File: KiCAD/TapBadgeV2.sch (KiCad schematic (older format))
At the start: 15 parts, among them M101 G0832013D, U101 DRV2605

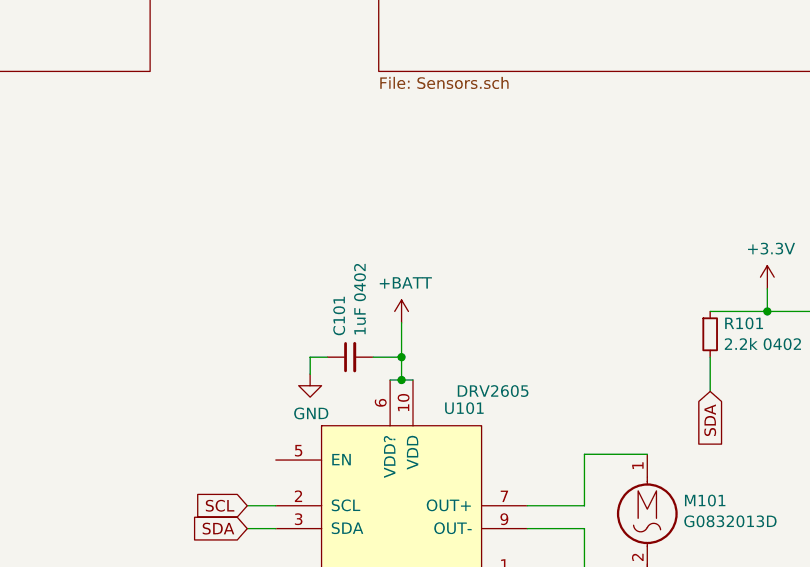
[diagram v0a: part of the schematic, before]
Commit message: Continue work on Schematics
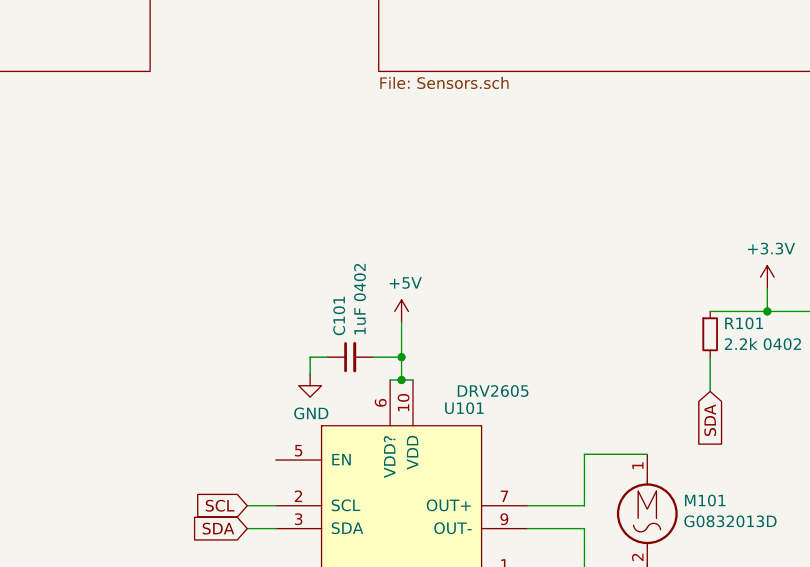
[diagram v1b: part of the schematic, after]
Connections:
- net +BATT renamed +5V
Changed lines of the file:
@@
 $Descr A4 11693 8268
 encoding utf-8
-Sheet 1 6
+Sheet 1 7
 Title ""
 Date ""
@@
 Wire Wire Line
 	7550 4800 7825 4800
-$Comp
-L power:+BATT #PWR0136
-U 1 1 60F9587F
-P 6750 4225
-F 0 "#PWR0136" H 6750 4075 50  0001 C CNN
-F 1 "+BATT" H 6765 4398 50  0000 C CNN
-F 2 "" H 6750 4225 50  0001 C CNN
-F 3 "" H 6750 4225 50  0001 C CNN
-	1    6750 4225
-	1    0    0    -1
-$EndComp
-Wire Wire Line
-	6750 4225 6750 4375
 Wire Wire Line
 	6750 4475 6700 4475
@@
 Wire Wire Line
 	2400 4675 2450 4675
-Text GLabel 2400 4575 1    50   Input ~ 0
-VGLOW
 $Comp
 L Device:C_Small C?
@@
 F1 "OLED_Panel.sch" 50
 $EndSheet
+$Comp
+L power:+5V #PWR0108
+U 1 1 610BED46
+P 6750 4225
+F 0 "#PWR0108" H 6750 4075 50  0001 C CNN
+F 1 "+5V" H 6765 4398 50  0000 C CNN
+F 2 "" H 6750 4225 50  0001 C CNN
+F 3 "" H 6750 4225 50  0001 C CNN
+	1    6750 4225
+	1    0    0    -1
+$EndComp
+Wire Wire Line
+	6750 4225 6750 4375
+Text GLabel 2400 4575 1    50   Input ~ 0
+VGLOW
 $EndSCHEMATC

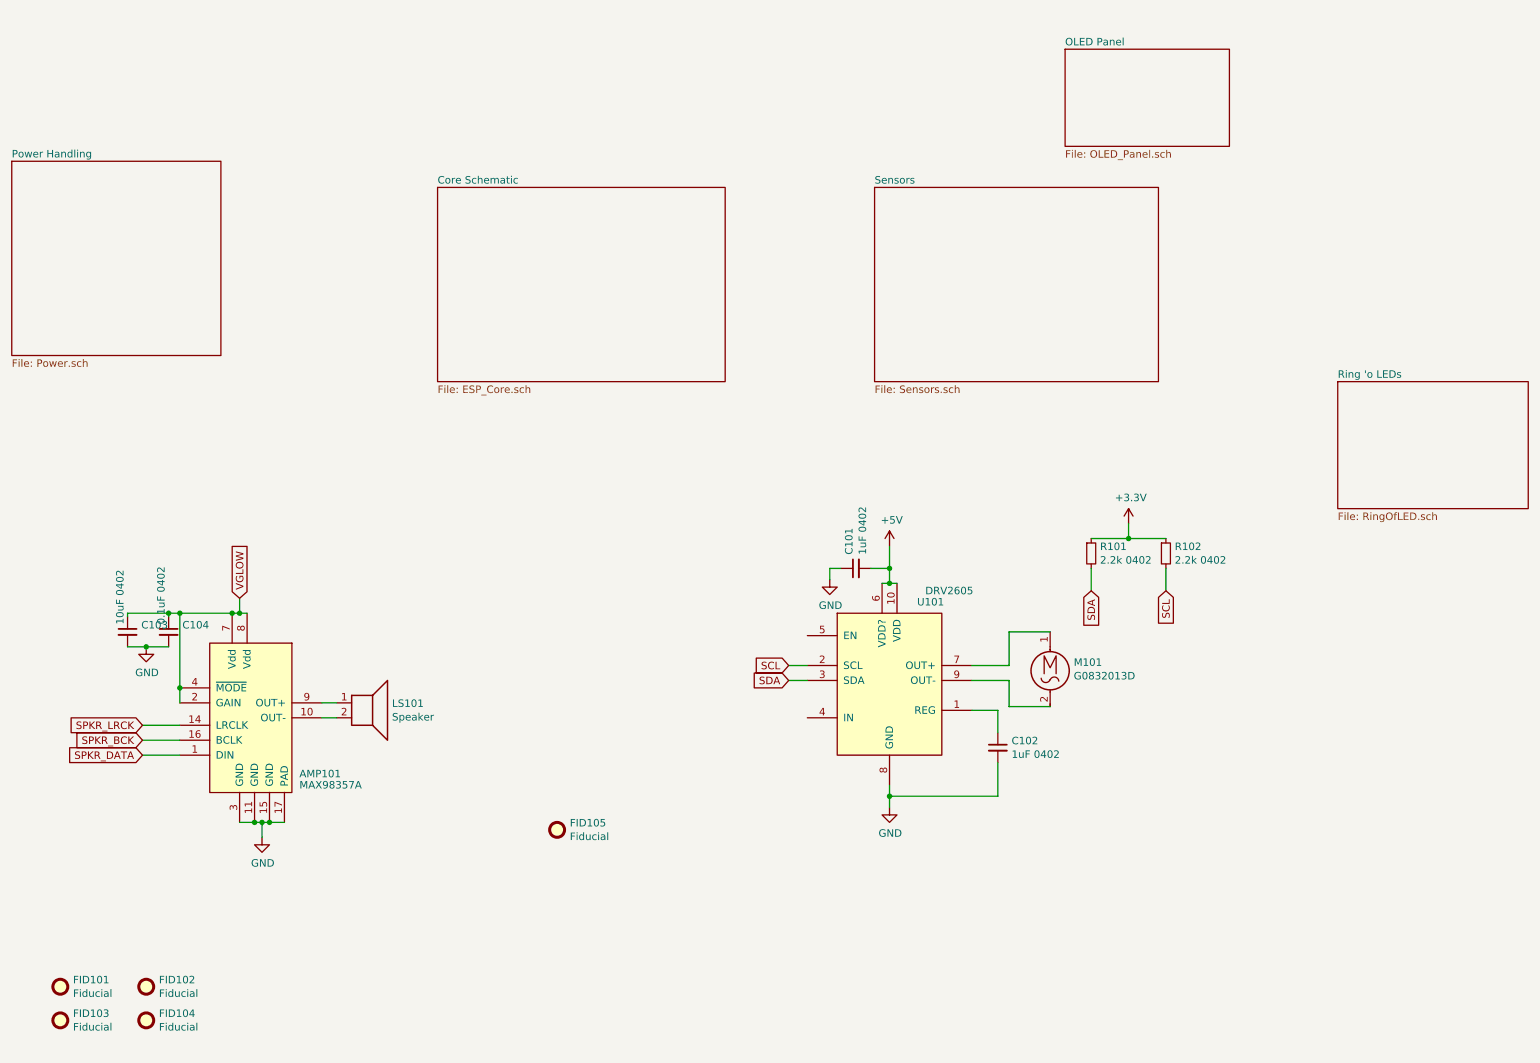
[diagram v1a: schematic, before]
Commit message: Add STM32 base circuit for power control and USB, also a lot of other things
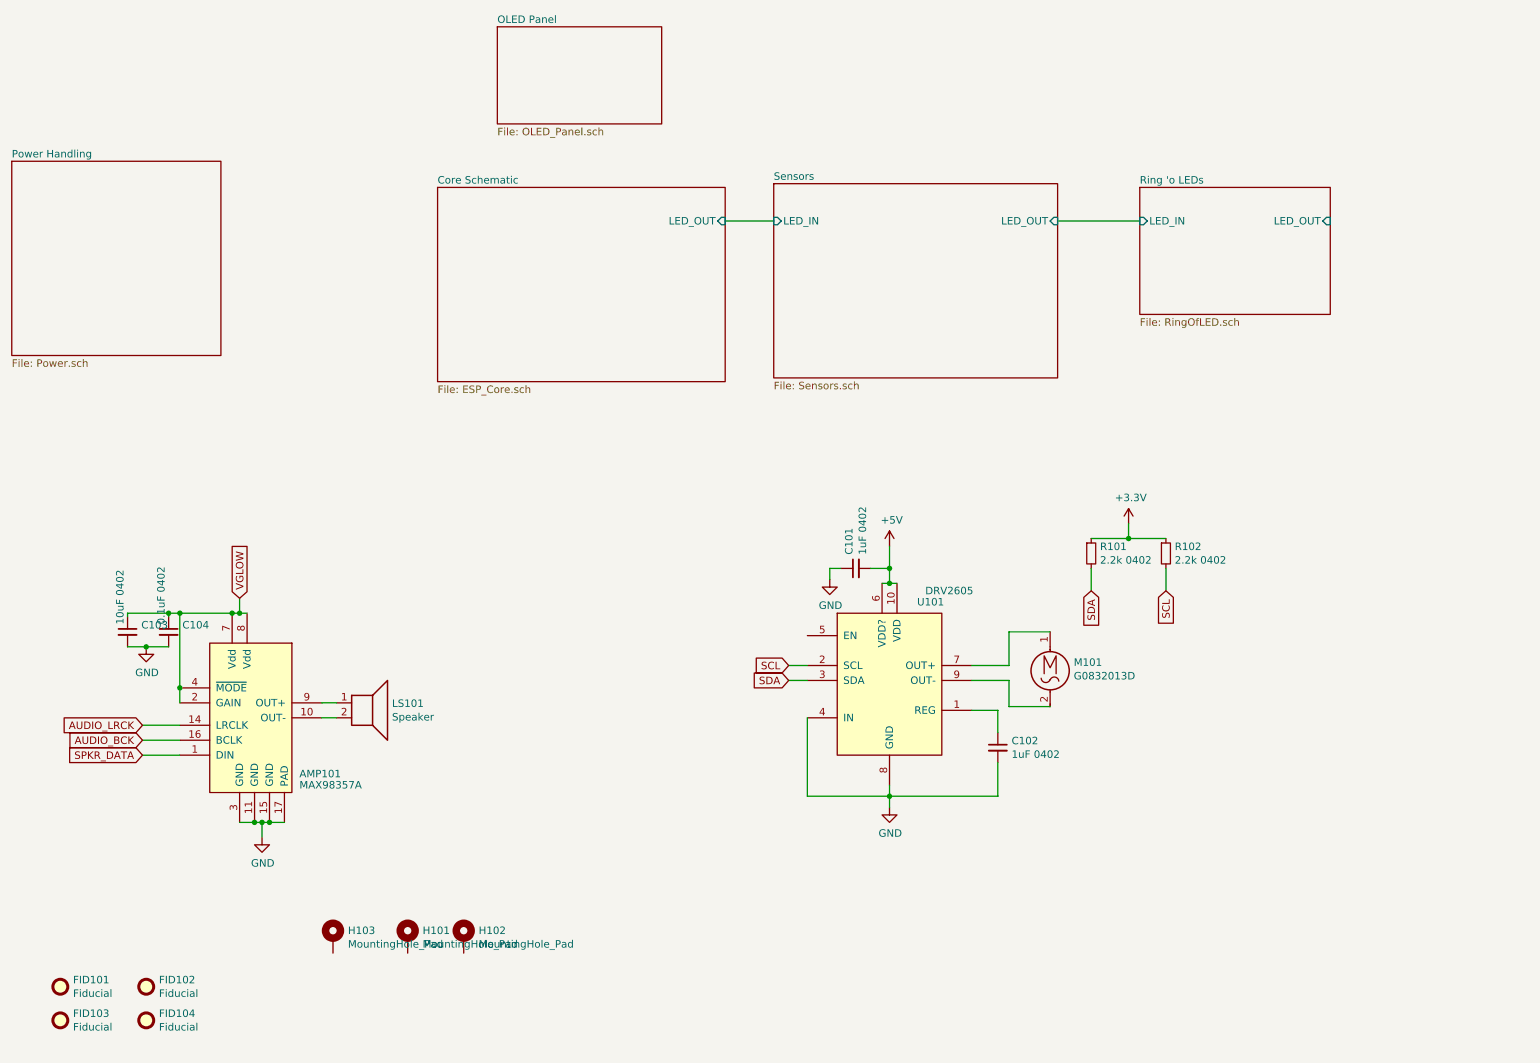
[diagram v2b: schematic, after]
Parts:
- removed FID105: Fiducial, MountingHole:MountingHole_2.2mm_M2_DIN965_Pad, symbol Mechanical:Fiducial
- added H101, H102, H103: MountingHole_Pad, XasPrints:MountingHole_1.5mm_M1_Pad_Via, symbol Mechanical:MountingHole_Pad
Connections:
- net GND: now also U101.4 (IN)
- net SPKR_BCK renamed AUDIO_BCK
- net SPKR_LRCK renamed AUDIO_LRCK
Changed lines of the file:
@@
 $Descr A4 11693 8268
 encoding utf-8
-Sheet 1 7
+Sheet 1 6
 Title ""
 Date ""
@@
 F0 "Core Schematic" 50
 F1 "ESP_Core.sch" 50
+F2 "LED_OUT" I R 5650 2050 50
 $EndSheet
 $Sheet
@@
 	8100 4375 8100 4525
 $Sheet
-S 6650 1825 1900 1300
+S 5975 1800 1900 1300
 U 60F2BC2A
 F0 "Sensors" 50
 F1 "Sensors.sch" 50
+F2 "LED_IN" I L 5975 2050 50
+F3 "LED_OUT" I R 7875 2050 50
 $EndSheet
 $Comp
@@
 	1    0    0    -1
 $EndComp
-$Sheet
-S 9750 3125 1275 850
-U 60F9A292
-F0 "Ring 'o LEDs" 50
-F1 "RingOfLED.sch" 50
-$EndSheet
 $Comp
 L XasParts:MAX98357A AMP101
@@
 	1775 4900 1925 4900
 Text GLabel 1750 5425 0    50   Input ~ 0
-SPKR_LRCK
+AUDIO_LRCK
 Text GLabel 1750 5525 0    50   Input ~ 0
-SPKR_BCK
+AUDIO_BCK
 Text GLabel 1750 5625 0    50   Input ~ 0
 SPKR_DATA
@@
 Wire Wire Line
 	6075 5025 6200 5025
-$Comp
-L Mechanical:Fiducial FID105
-U 1 1 60FF59E3
-P 4525 6125
-F 0 "FID105" H 4610 6171 50  0000 L CNN
-F 1 "Fiducial" H 4610 6080 50  0000 L CNN
-F 2 "MountingHole:MountingHole_2.2mm_M2_DIN965_Pad" H 4525 6125 50  0001 C CNN
-F 3 "~" H 4525 6125 50  0001 C CNN
-	1    4525 6125
-	1    0    0    -1
-$EndComp
 $Sheet
-S 7925 900  1100 650
+S 4125 750  1100 650
 U 61017570
 F0 "OLED Panel" 50
@@
 Text GLabel 2400 4575 1    50   Input ~ 0
 VGLOW
+$Comp
+L Mechanical:MountingHole_Pad H102
+U 1 1 6109C258
+P 3900 6850
+F 0 "H102" H 4000 6901 50  0000 L CNN
+F 1 "MountingHole_Pad" H 4000 6810 50  0000 L CNN
+F 2 "XasPrints:MountingHole_1.5mm_M1_Pad_Via" H 3900 6850 50  0001 C CNN
+F 3 "~" H 3900 6850 50  0001 C CNN
+	1    3900 6850
+	1    0    0    -1
+$EndComp
+$Comp
+L Mechanical:MountingHole_Pad H101
+U 1 1 6109C6EA
+P 3525 6850
+F 0 "H101" H 3625 6901 50  0000 L CNN
+F 1 "MountingHole_Pad" H 3625 6810 50  0000 L CNN
+F 2 "XasPrints:MountingHole_1.5mm_M1_Pad_Via" H 3525 6850 50  0001 C CNN
+F 3 "~" H 3525 6850 50  0001 C CNN
+	1    3525 6850
+	1    0    0    -1
+$EndComp
+$Comp
+L Mechanical:MountingHole_Pad H103
+U 1 1 610C5CB3
+P 3025 6850
+F 0 "H103" H 3125 6901 50  0000 L CNN
+F 1 "MountingHole_Pad" H 3125 6810 50  0000 L CNN
+F 2 "XasPrints:MountingHole_1.5mm_M1_Pad_Via" H 3025 6850 50  0001 C CNN
+F 3 "~" H 3025 6850 50  0001 C CNN
+	1    3025 6850
+	1    0    0    -1
+$EndComp
+Wire Wire Line
+	5650 2050 5975 2050
+$Sheet
+S 8425 1825 1275 850
+U 60F9A292
+F0 "Ring 'o LEDs" 50
+F1 "RingOfLED.sch" 50
+F2 "LED_IN" I L 8425 2050 50
+F3 "LED_OUT" I R 9700 2050 50
+$EndSheet
+Wire Wire Line
+	6200 5900 6750 5900
+Wire Wire Line
+	6200 5375 6200 5900
+Wire Wire Line
+	7875 2050 8425 2050
 $EndSCHEMATC

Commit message: Continue work on TapV2's schematic, almost completing it!
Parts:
- removed FID103: Fiducial, Fiducial:Fiducial_1mm_Mask2mm, symbol Mechanical:Fiducial
- C103: value 10uF 0402 -> 10uF 0603; footprint Capacitor_SMD:C_0402_1005Metric -> Capacitor_SMD:C_0603_1608Metric
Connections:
- net +5V: now also U101.5 (EN)
- net GND: now also H101.1, H102.1, H103.1
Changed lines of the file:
@@
-$EndComp
-$Comp
-L Mechanical:Fiducial FID103
-U 1 1 60F99347
-P 1200 7400
-F 0 "FID103" H 1285 7446 50  0000 L CNN
-F 1 "Fiducial" H 1285 7355 50  0000 L CNN
-F 2 "Fiducial:Fiducial_1mm_Mask2mm" H 1200 7400 50  0001 C CNN
-F 3 "~" H 1200 7400 50  0001 C CNN
-	1    1200 7400
-	1    0    0    -1
 $EndComp
 $Comp
@@
 AR Path="/60FB3667" Ref="C103"  Part="1"
 F 0 "C103" H 1742 4846 50  0000 L CNN
-F 1 "10uF 0402" V 1600 4850 50  0000 L CNN
-F 2 "Capacitor_SMD:C_0402_1005Metric" H 1650 4800 50  0001 C CNN
+F 1 "10uF 0603" V 1600 4850 50  0000 L CNN
+F 2 "Capacitor_SMD:C_0603_1608Metric" H 1650 4800 50  0001 C CNN
 F 3 "~" H 1650 4800 50  0001 C CNN
 	1    1650 4800
@@
 Wire Wire Line
 	7875 2050 8425 2050
+Wire Wire Line
+	3025 6950 3025 7025
+Wire Wire Line
+	3025 7025 3525 7025
+Wire Wire Line
+	3900 7025 3900 6950
+Wire Wire Line
+	3525 6950 3525 7025
+Connection ~ 3525 7025
+Wire Wire Line
+	3525 7025 3900 7025
+$Comp
+L power:GND #PWR0154
+U 1 1 6136A261
+P 3525 7100
+F 0 "#PWR0154" H 3525 6850 50  0001 C CNN
+F 1 "GND" H 3530 6927 50  0000 C CNN
+F 2 "" H 3525 7100 50  0001 C CNN
+F 3 "" H 3525 7100 50  0001 C CNN
+	1    3525 7100
+	1    0    0    -1
+$EndComp
+Wire Wire Line
+	3525 7100 3525 7025
+$Comp
+L power:+5V #PWR0157
+U 1 1 613C2046
+P 6100 4800
+F 0 "#PWR0157" H 6100 4650 50  0001 C CNN
+F 1 "+5V" H 6115 4973 50  0000 C CNN
+F 2 "" H 6100 4800 50  0001 C CNN
+F 3 "" H 6100 4800 50  0001 C CNN
+	1    6100 4800
+	1    0    0    -1
+$EndComp
+Wire Wire Line
+	6100 4800 6100 4825
+Wire Wire Line
+	6100 4825 6200 4825
 $EndSCHEMATC

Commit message: Finalize PCB schematics
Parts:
- added SYM101: SYM_Radioactive_Large, XasPrints:DragonIcon_7mm_Solder, symbol Graphic:SYM_Radioactive_Large
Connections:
- net +5V: now also AMP101.2 (GAIN), AMP101.7 (Vdd), AMP101.8 (Vdd), C103.1, C104.1
- net VGLOW: no longer AMP101.2 (GAIN), AMP101.7 (Vdd), AMP101.8 (Vdd), C103.1, C104.1
- no-connect marks 0 -> 1
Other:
- note added: "7bit addr: 0x5A"
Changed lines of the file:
@@
 Wire Wire Line
 	1925 4700 1925 4675
-Wire Wire Line
-	1925 4675 2000 4675
 Connection ~ 2350 4675
 Wire Wire Line
@@
 Wire Wire Line
 	1750 5425 2000 5425
-Wire Wire Line
-	2000 5175 2000 4675
-Connection ~ 2000 4675
-Wire Wire Line
-	2000 4675 2350 4675
-Wire Wire Line
-	2000 5275 2000 5175
-Connection ~ 2000 5175
 Text GLabel 6075 5025 0    50   Input ~ 0
 SCL
@@
 Wire Wire Line
 	6750 4225 6750 4375
-Text GLabel 2400 4575 1    50   Input ~ 0
+Text GLabel 1725 5175 0    50   Input ~ 0
 VGLOW
 $Comp
@@
 Wire Wire Line
 	6100 4825 6200 4825
+Text Notes 6925 4375 0    50   ~ 0
+7bit addr: 0x5A
+$Comp
+L power:+5V #PWR?
+U 1 1 61451818
+P 2400 4575
+AR Path="/60EE6959/61451818" Ref="#PWR?"  Part="1"
+AR Path="/61451818" Ref="#PWR0159"  Part="1"
+F 0 "#PWR0159" H 2400 4425 50  0001 C CNN
+F 1 "+5V" H 2415 4748 50  0000 C CNN
+F 2 "" H 2400 4575 50  0001 C CNN
+F 3 "" H 2400 4575 50  0001 C CNN
+	1    2400 4575
+	1    0    0    -1
+$EndComp
+Wire Wire Line
+	1925 4675 2100 4675
+Wire Wire Line
+	2000 5175 1725 5175
+Wire Wire Line
+	2000 5275 1925 5275
+Wire Wire Line
+	1925 5275 1925 5025
+Wire Wire Line
+	1925 5025 2100 5025
+Wire Wire Line
+	2100 5025 2100 4675
+Connection ~ 2100 4675
+Wire Wire Line
+	2100 4675 2350 4675
+$Comp
+L Graphic:SYM_Radioactive_Large SYM101
+U 1 1 61459890
+P 6125 7475
+F 0 "SYM101" H 6220 7755 50  0001 C CNN
+F 1 "SYM_Radioactive_Large" H 6220 7305 50  0001 C CNN
+F 2 "XasPrints:DragonIcon_7mm_Solder" H 6220 7355 50  0001 C CNN
+F 3 "~" H 6250 7355 50  0001 C CNN
+	1    6125 7475
+	1    0    0    -1
+$EndComp
+Wire Wire Line
+	9700 2050 9900 2050
+NoConn ~ 9900 2050
 $EndSCHEMATC
